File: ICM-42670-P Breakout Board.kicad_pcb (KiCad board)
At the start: 2 copper layers, 18 x 26.5 mm, 10 parts, among them J2 Conn_01x09_Pin, U1 ICM-42670-P, U2 MCP1700x-330xxTT

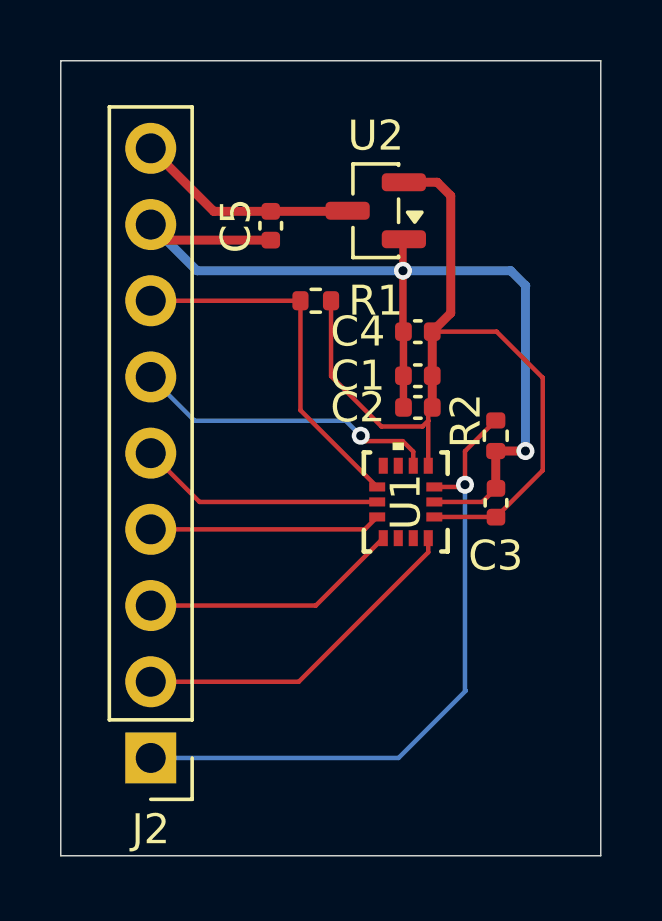
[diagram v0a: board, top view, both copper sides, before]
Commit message: Added SilkScreen Text
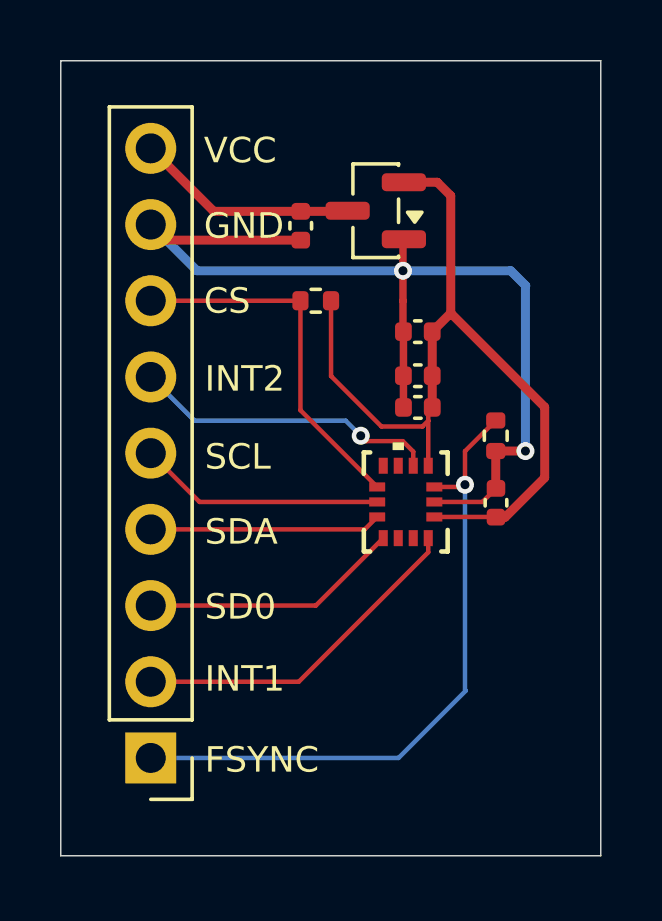
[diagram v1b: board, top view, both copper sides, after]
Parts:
- moved C5 1.00 mm to (129.0, 76.5)
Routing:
- net GND: track 33.2 -> 34.2 mm
- net /3V3_Clean: track 29.4 -> 28.7 mm
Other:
- board text added: "CS"
- board text added: "FSYNC"
- board text added: "GND"
- board text added: "INT1"
- board text added: "INT2"
- board text added: "SCL"
- board text added: "SD0"
- board text added: "SDA"
- board text added: "VCC"

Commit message: Wired LED
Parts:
- added D1: LED, LED_SMD:LED_0603_1608Metric, F.Cu at (136.4, 92.2)
- added R3: 120Ω, Resistor_SMD:R_0402_1005Metric, F.Cu at (134.5, 92.5)
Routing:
- net GND: track 34.2 -> 41.9 mm, vias 2 -> 3
- net /3V3_Clean: track 28.7 -> 34.9 mm
- net Net-(D1-A): track 0.00 -> 1.96 mm
